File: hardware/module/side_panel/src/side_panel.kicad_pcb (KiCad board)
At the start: 2 copper layers, 96 x 120.2 mm, 36 parts, among them J1 Top Connector, J2 Bottom Connecor, J3 Conn_01x05, J4 Conn_01x09, M1 GA12-N20 12V 60rpm, Q1 AP2302B, U1 QRE1113GR, U10 NUP4202, U2 QRE1113GR, U3 QRE1113GR, U4 QRE1113GR, U5 QRE1113GR, U6 QRE1113GR, U7 PY32F003F1xPx, U8 L9110S, U9 74LVC1G66

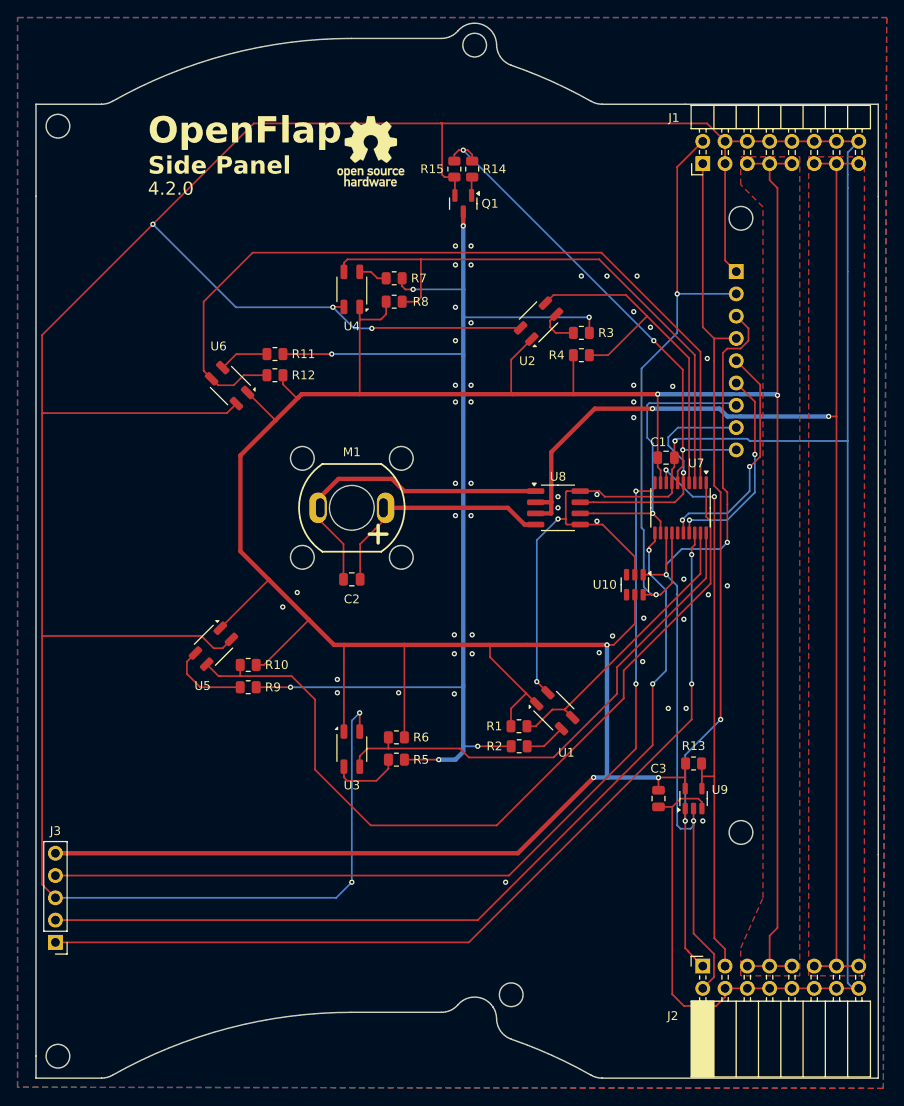
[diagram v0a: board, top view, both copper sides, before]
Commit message: changed hole patern encoder wheel
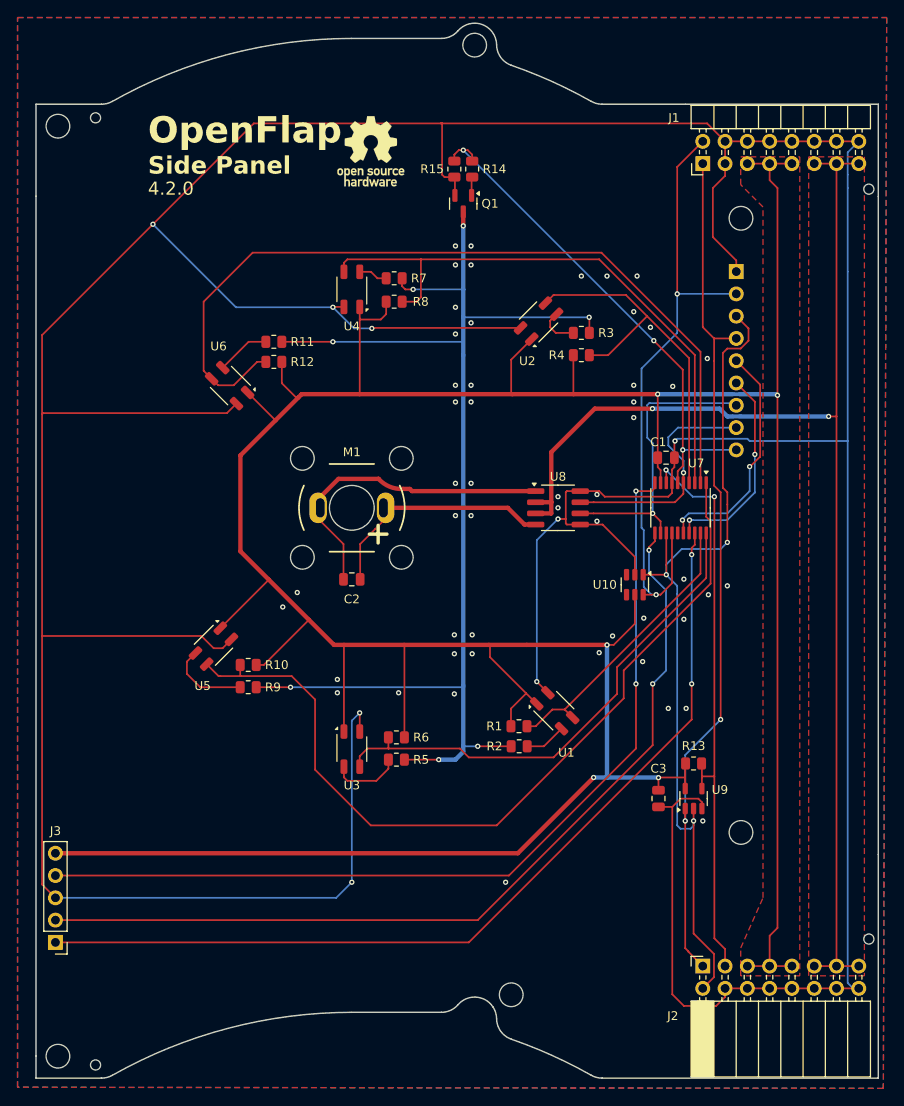
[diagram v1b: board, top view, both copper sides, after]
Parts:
- added H1: MountingHole, MountingHole:MountingHole_2.7mm, F.Cu at (63.4, 88.7)
- added H10: MountingHole, MountingHole:MountingHole_2.7mm, F.Cu at (91.3, 126.5)
- added H2: MountingHole, MountingHole:MountingHole_2.7mm, F.Cu at (110.9, 79.4)
- added H3: MountingHole, MountingHole:MountingHole_2.7mm, F.Cu at (141.3, 99.2)
- added H4: MountingHole, MountingHole:MountingHole_2.7mm, F.Cu at (63.4, 194.7)
- added H5: MountingHole, MountingHole:MountingHole_2.7mm, F.Cu at (141.3, 169.2)
- added H6: MountingHole, MountingHole:MountingHole_2.7mm, F.Cu at (115.1, 187.7)
- added H7: MountingHole, MountingHole:MountingHole_2.7mm, F.Cu at (102.6, 137.8)
- added H8: MountingHole, MountingHole:MountingHole_2.7mm, F.Cu at (102.6, 126.5)
- added H9: MountingHole, MountingHole:MountingHole_2.7mm, F.Cu at (91.3, 137.8)
- added TH1: TOOLING_HOLE, ToolingHole:TOOLING_HOLE, F.Cu at (67.7, 195.7)
- added TH2: TOOLING_HOLE, ToolingHole:TOOLING_HOLE, F.Cu at (155.9, 181.3)
- added TH3: TOOLING_HOLE, ToolingHole:TOOLING_HOLE, F.Cu at (155.9, 95.9)
- added TH4: TOOLING_HOLE, ToolingHole:TOOLING_HOLE, F.Cu at (67.7, 87.7)
- moved R12 1.53 mm to (88.1, 115.5)
- moved R11 1.40 mm to (88.1, 113.3)
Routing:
- net Net-(M1--): track 37.9 -> 34.7 mm
- net +5V: track 420.4 -> 421.9 mm
- net GND: track 567.7 -> 568.9 mm
- net /IR Sens Ch 6: track 94.8 -> 95.3 mm
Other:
- outline, holes or cut-outs redrawn

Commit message: Increase encoder LED current to 70mA and make make two pairs of 3 to reduce power draw
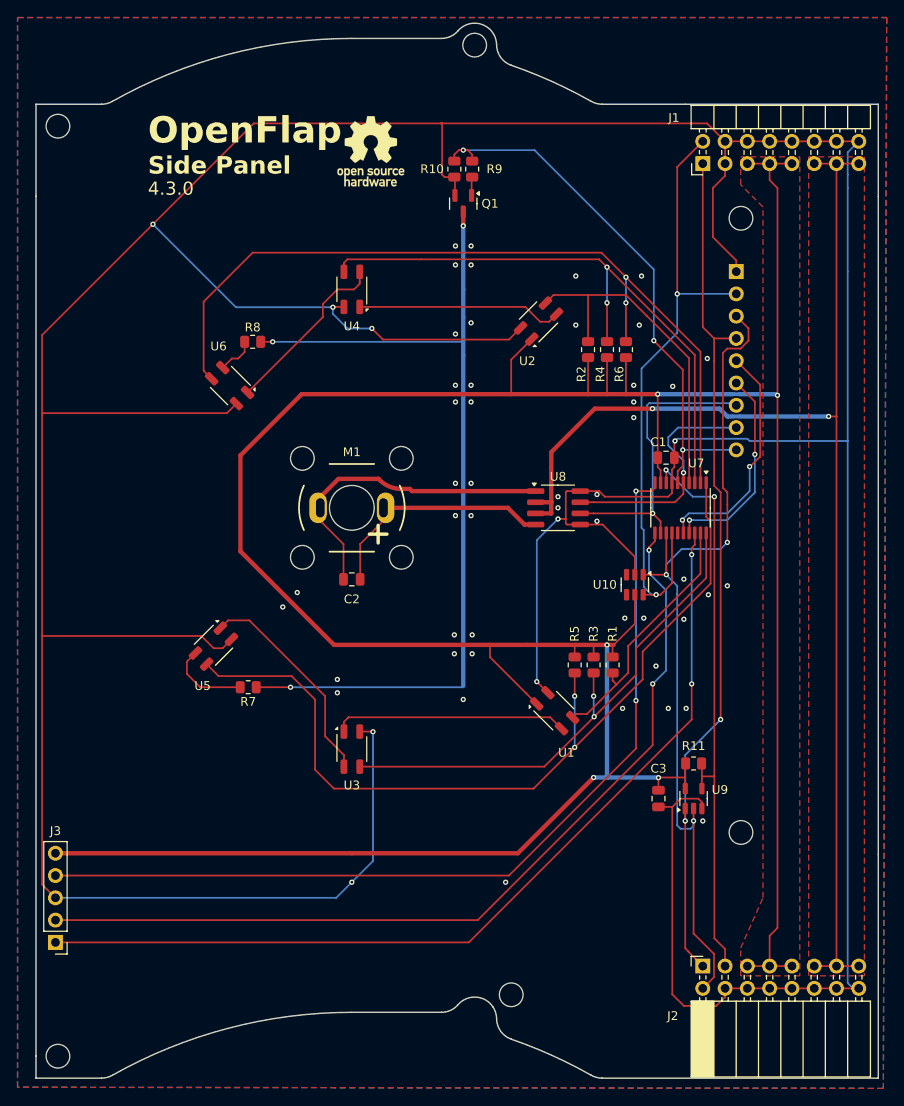
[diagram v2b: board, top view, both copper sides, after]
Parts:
- removed the R10 at (85.1, 150.1)
- removed the R11 at (88.1, 113.3)
- removed R12: 20K, Resistor_SMD:R_0805_2012Metric
- removed the R9 at (85.1, 152.6)
- removed TH1, TH2, TH3, TH4: TOOLING_HOLE, ToolingHole:TOOLING_HOLE
- R2, R3, R5: value 100R -> 20K
- R7: value 100R -> 20R
- R8: value 20K -> 20R
- moved R6 51.4 mm to (128.2, 114.1), turned to 90 degrees
- moved R7 49.5 mm to (85.1, 152.6)
- moved R2 45.9 mm to (123.9, 114.1), turned to 90 degrees
- moved R3 37.9 mm to (124.5, 150.1), turned to -90 degrees
- moved R5 23.0 mm to (122.3, 150.1), turned to -90 degrees
- moved R8 16.8 mm to (85.6, 113.3)
- moved R1 12.8 mm to (126.7, 150.1), turned to -90 degrees
- moved R4 2.99 mm to (126.0, 114.1), turned to 90 degrees
- renumbered R15 to R10, R13 to R11, R14 to R9
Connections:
- R2 pad 1: Net-(Q1-D) -> +5V
- R2 pad 2: Net-(U1-K) -> /IR Sens Ch 2
- R3 pad 1: Net-(Q1-D) -> +5V
- R3 pad 2: Net-(U2-K) -> /IR Sens Ch 3
- R4 pad 2: /IR Sens Ch 2 -> /IR Sens Ch 4
- R5 pad 1: Net-(Q1-D) -> +5V
- R5 pad 2: Net-(U3-K) -> /IR Sens Ch 5
- R6 pad 2: /IR Sens Ch 3 -> /IR Sens Ch 6
- R7 pad 2: Net-(U4-K) -> Net-(U5-K)
- R8 pad 1: +5V -> Net-(U6-K)
- R8 pad 2: /IR Sens Ch 4 -> Net-(Q1-D)
- U3 pad 1: +5V -> Net-(U1-K)
- U4 pad 1: +5V -> Net-(U2-K)
- U5 pad 1: +5V -> Net-(U3-K)
- U6 pad 1: +5V -> Net-(U4-K)
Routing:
- net +5V: track 421.9 -> 369.1 mm
- net Net-(Q1-D): track 142.6 -> 100.8 mm, vias 7 -> 3
- net Net-(U1-K): track 4.74 -> 26.7 mm
- net Net-(U2-K): track 4.70 -> 23.5 mm
- net Net-(U4-K): track 3.32 -> 20.2 mm
- net Net-(U3-K): track 8.06 -> 24.8 mm
- net /IR Sense LED: track 58.5 -> 63.3 mm
- net /IR Sens Ch 5: track 96.0 -> 99.7 mm, vias 0 -> 2
- net /IR Sens Ch 1: track 32.9 -> 29.3 mm
- net /IR Sens Ch 2: track 42.4 -> 39.2 mm
- net /IR Sens Ch 3: track 58.1 -> 60.3 mm, vias 0 -> 2
- net /IR Sens Ch 4: track 66.9 -> 68.7 mm, vias 0 -> 2
- net Net-(U6-K): track 6.12 -> 4.39 mm
- net GND: track 568.9 -> 568.3 mm, vias 59 -> 56
- net /IR Sens Ch 6: track 95.3 -> 95.1 mm, vias 0 -> 2

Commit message: Change from absolute encoder to incremental encoder.
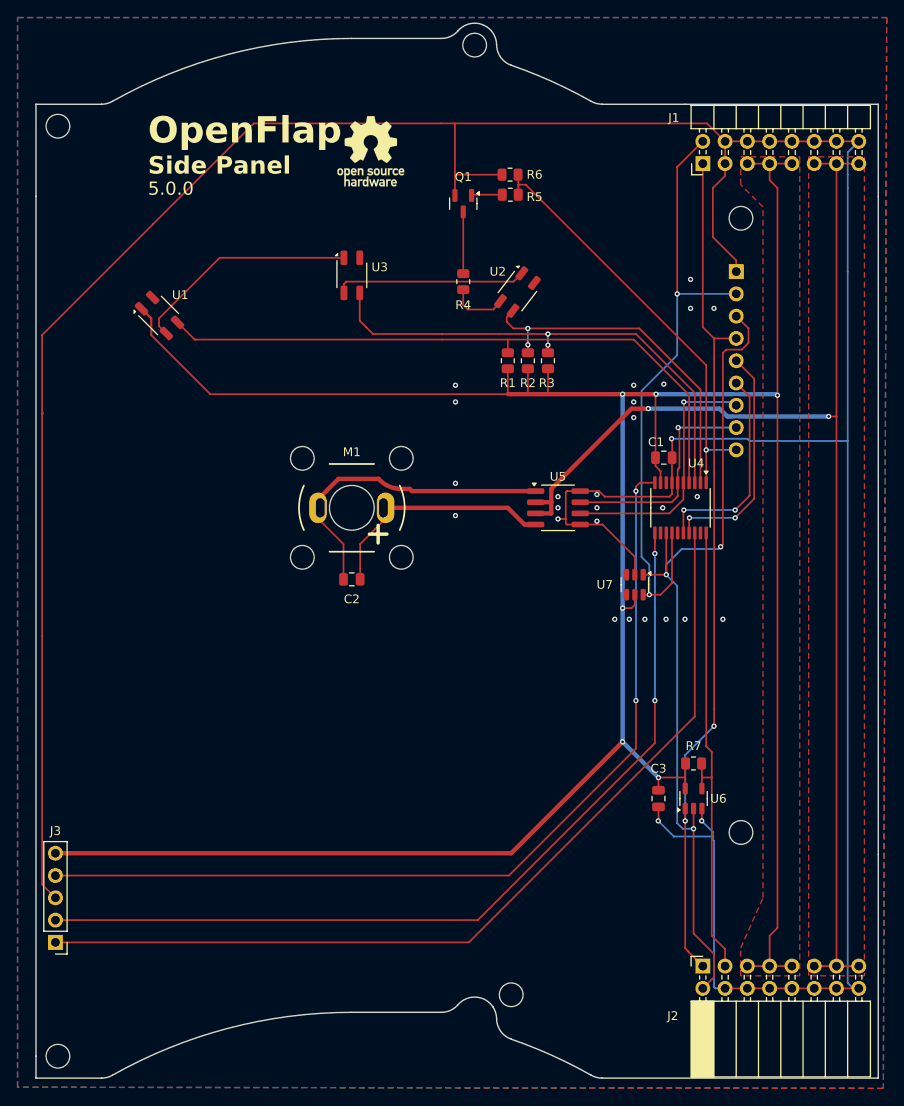
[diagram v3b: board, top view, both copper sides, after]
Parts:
- removed the R5 at (122.3, 150.1)
- removed the R6 at (128.2, 114.1)
- removed the R7 at (85.1, 152.6)
- removed R8: 20R, Resistor_SMD:R_0805_2012Metric
- removed the U4 at (96.9, 107.3)
- removed the U5 at (81.2, 148.0)
- removed the U6 at (83.0, 118.3)
- R4: value 20K -> 20R
- U1, U2, U3: value QRE1113GR -> ITR8307
- moved U1 63.7 mm to (75.0, 110.3)
- moved U3 54.0 mm to (96.9, 105.7)
- moved R1 36.7 mm to (114.7, 115.4), turned to 90 degrees
- moved R3 35.1 mm to (119.3, 115.4), turned to 90 degrees
- moved R4 18.1 mm to (109.6, 106.4)
- moved R2 6.97 mm to (117.0, 115.4)
- moved R6 6.38 mm to (115.0, 94.2), turned to 180 degrees
- moved R5 5.23 mm to (115.0, 96.5), turned to 180 degrees
- moved U2 4.10 mm to (115.8, 107.6), turned to -37.5 degrees
- moved C1 0.25 mm to (132.5, 126.5)
- renumbered R9 to R5, R10 to R6, R11 to R7, U7 to U4, U8 to U5, U9 to U6, U10 to U7
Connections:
- J4 pad 9: /IR Sense LED -> /IR Sens LED
- R1 pad 2: /IR Sens Ch 1 -> /IR Sens A
- R2 pad 2: /IR Sens Ch 2 -> /IR Sens B
- R3 pad 2: /IR Sens Ch 3 -> /IR Sens Z
- R4 pad 1: +5V -> Net-(U2-K)
- R4 pad 2: /IR Sens Ch 4 -> Net-(Q1-D)
- R5 pad 1: /IR Sense LED -> /IR Sens LED
- R6 pad 1: /IR Sense LED -> /IR Sens LED
- U1 pad 3: /IR Sens Ch 1 -> /IR Sens A
- U2 pad 1: +5V -> Net-(U2-A)
- U2 pad 3: /IR Sens Ch 2 -> /IR Sens B
- U3 pad 2: Net-(U3-K) -> Net-(U2-A)
- U3 pad 3: /IR Sens Ch 3 -> /IR Sens Z
- U4 pad 1: /IR Sens Ch 5 -> /IR Sens LED
- U4 pad 12: /Motor IN_A -> unconnected-(U4-PB5-Pad12)
- U4 pad 16: /Debug Pin 1 -> /Debug Pin 2
- U4 pad 17: /Debug Pin 2 -> /Debug Pin 1
- U4 pad 19: /IR Sens Ch 1 -> unconnected-(U4-PA0-Pad19)
- U4 pad 2: /IR Sens Ch 6 -> /IR Sens B
- U4 pad 20: /IR Sens Ch 3 -> /Column End
- U4 pad 3: /IR Sens Ch 4 -> /IR Sens Z
- U4 pad 4: /IR Sens Ch 2 -> /IR Sens A
- U4 pad 5: /Motor IN_B -> /Motor IN_A
- U4 pad 6: /IR Sense LED -> /Motor IN_B
- U4 pad 8: /Column End -> unconnected-(U4-PA12-Pad8)
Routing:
- net GND: track 568.3 -> 397.8 mm, vias 56 -> 28
- net /IR Sens Ch 5: track 99.7 -> 0.00 mm, vias 2 -> 0
- net /IR Sens Ch 6: track 95.1 -> 0.00 mm, vias 2 -> 0
- net Net-(Q1-D): track 100.8 -> 7.04 mm, vias 3 -> 0
- net /IR Sens A: track 0.00 -> 73.2 mm
- net /IR Sens Ch 4: track 68.7 -> 0.00 mm, vias 2 -> 0
- net /IR Sense LED: track 63.3 -> 0.00 mm, vias 3 -> 0
- net /IR Sens Ch 3: track 60.3 -> 0.00 mm, vias 2 -> 0
- net /IR Sens Z: track 0.00 -> 57.1 mm, vias 0 -> 2
- net /IR Sens LED: track 0.00 -> 49.1 mm, vias 0 -> 1
- net +5V: track 369.1 -> 324.7 mm, vias 5 -> 6
- net /IR Sens B: track 0.00 -> 40.2 mm, vias 0 -> 2
- net /IR Sens Ch 2: track 39.2 -> 0.00 mm
- net /IR Sens Ch 1: track 29.3 -> 0.00 mm
- net Net-(U3-K): track 24.8 -> 0.00 mm
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
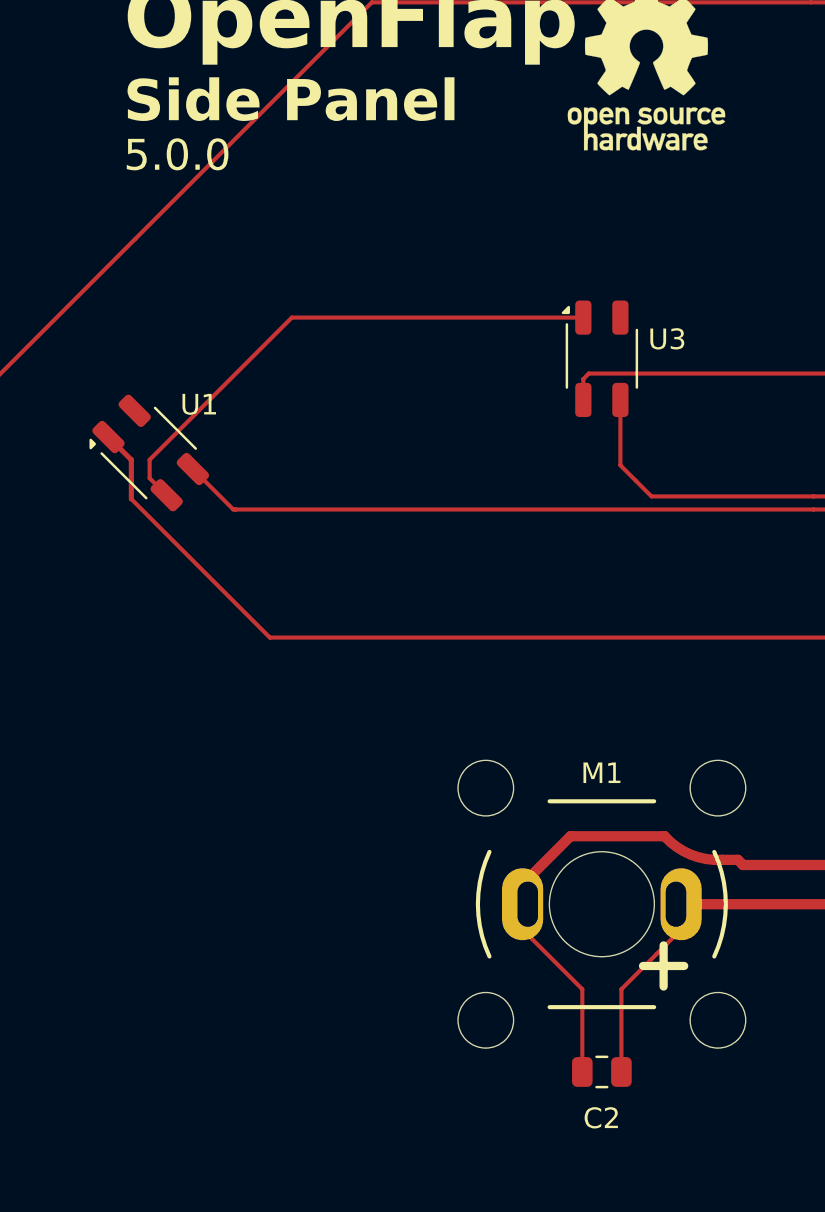
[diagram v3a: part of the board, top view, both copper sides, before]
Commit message: Side panel 5.0.1 swap motor polarity
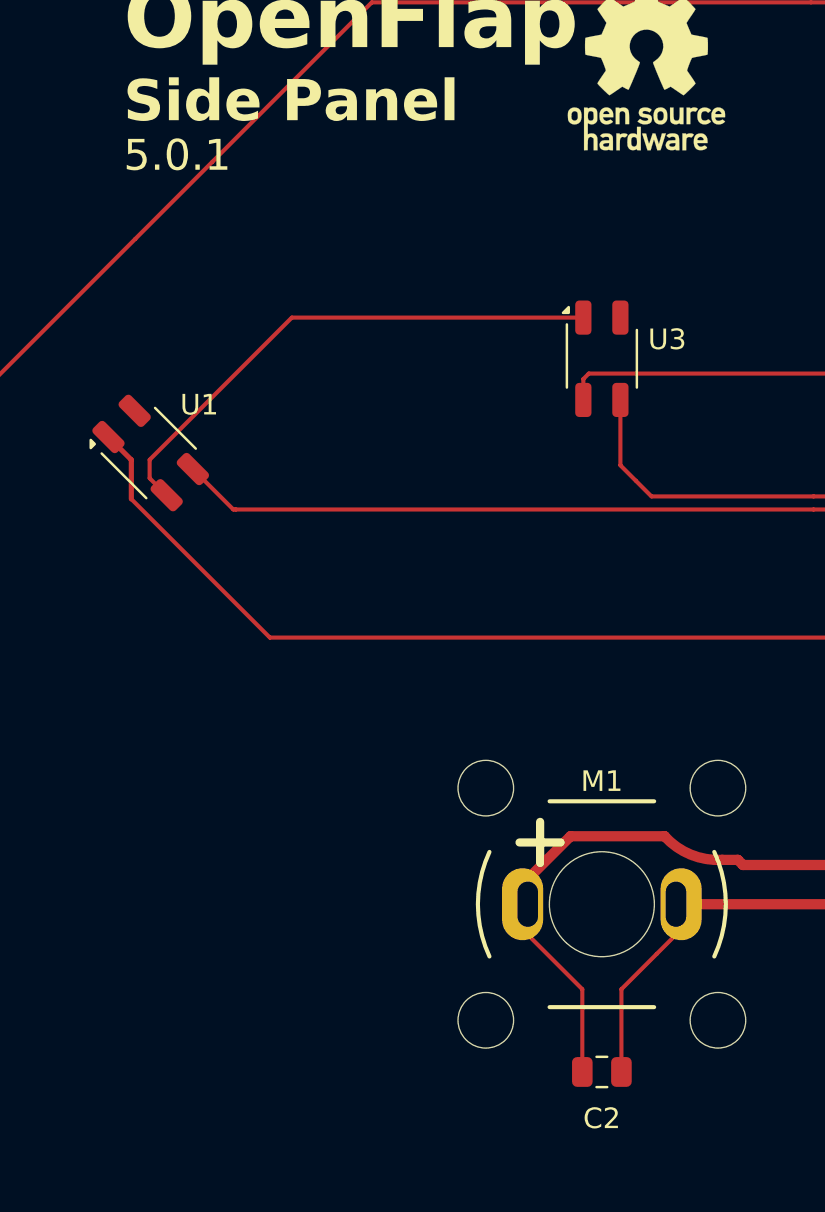
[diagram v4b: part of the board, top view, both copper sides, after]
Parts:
- turned C2 to 0 degrees
- turned M1 to 0 degrees
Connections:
- U5 pad 1: Net-(M1--) -> Net-(M1-+)
- U5 pad 4: Net-(M1-+) -> Net-(M1--)
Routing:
- net Net-(M1--): track 34.7 -> 28.9 mm
- net Net-(M1-+): track 28.9 -> 34.7 mm
